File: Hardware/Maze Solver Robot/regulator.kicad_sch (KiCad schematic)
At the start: 0 parts

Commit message: Voltage Regulator
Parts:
- added C?: 220u, symbol Device:C_Polarized_Small_US
- added C?: 10u, symbol Device:C_Polarized_Small_US
- added R?: 240, symbol Device:R
- added R?: 390, symbol Device:R
- added U?: LM317L_SOT-89, Package_TO_SOT_SMD:SOT-89-3, symbol Regulator_Linear:LM317L_SOT-89
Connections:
- new net: R?.1, R?.2, U?.1 (ADJ)
- new net 3.3V: C?.1, R?.1, U?.2 (VO)
- new net GND: C?.2, C?.2, R?.2
- new net Input (Battery?): C?.1, U?.3 (VI)
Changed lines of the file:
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@@
 (kicad_sch (version 20211123) (generator eeschema)
   (paper "A4")
+  (junction (at 142.875 78.74) (diameter 0) (color 0 0 0 0)
+  )
+  (junction (at 170.815 64.77) (diameter 0) (color 0 0 0 0)
+  )
+  (junction (at 142.875 93.345) (diameter 0) (color 0 0 0 0)
+  )
+  (junction (at 159.385 64.77) (diameter 0) (color 0 0 0 0)
+  )
+  (junction (at 128.27 64.77) (diameter 0) (color 0 0 0 0)
+  )
+  (junction (at 128.27 93.345) (diameter 0) (color 0 0 0 0)
+  )
+  (wire (pts (xy 122.555 64.77) (xy 128.27 64.77))
+    (stroke (width 0) (type default) (color 0 0 0 0))
+  )
+  (wire (pts (xy 159.385 77.47) (xy 159.385 78.74))
+    (stroke (width 0) (type default) (color 0 0 0 0))
+  )
+  (wire (pts (xy 142.875 78.74) (xy 159.385 78.74))
+    (stroke (width 0) (type default) (color 0 0 0 0))
+  )
+  (wire (pts (xy 159.385 64.77) (xy 159.385 69.85))
+    (stroke (width 0) (type default) (color 0 0 0 0))
+  )
+  (wire (pts (xy 170.815 64.77) (xy 170.815 71.12))
+    (stroke (width 0) (type default) (color 0 0 0 0))
+  )
+  (wire (pts (xy 128.27 93.345) (xy 128.27 95.25))
+    (stroke (width 0) (type default) (color 0 0 0 0))
+  )
+  (wire (pts (xy 128.27 64.77) (xy 128.27 71.755))
+    (stroke (width 0) (type default) (color 0 0 0 0))
+  )
+  (wire (pts (xy 128.27 76.835) (xy 128.27 93.345))
+    (stroke (width 0) (type default) (color 0 0 0 0))
+  )
+  (wire (pts (xy 159.385 64.77) (xy 170.815 64.77))
+    (stroke (width 0) (type default) (color 0 0 0 0))
+  )
+  (wire (pts (xy 170.815 93.345) (xy 170.815 76.2))
+    (stroke (width 0) (type default) (color 0 0 0 0))
+  )
+  (wire (pts (xy 142.875 93.345) (xy 170.815 93.345))
+    (stroke (width 0) (type default) (color 0 0 0 0))
+  )
+  (wire (pts (xy 170.815 64.77) (xy 177.165 64.77))
+    (stroke (width 0) (type default) (color 0 0 0 0))
+  )
+  (wire (pts (xy 128.27 93.345) (xy 142.875 93.345))
+    (stroke (width 0) (type default) (color 0 0 0 0))
+  )
+  (wire (pts (xy 128.27 64.77) (xy 135.255 64.77))
+    (stroke (width 0) (type default) (color 0 0 0 0))
+  )
+  (wire (pts (xy 142.875 90.805) (xy 142.875 93.345))
+    (stroke (width 0) (type default) (color 0 0 0 0))
+  )
+  (wire (pts (xy 142.875 78.74) (xy 142.875 83.185))
+    (stroke (width 0) (type default) (color 0 0 0 0))
+  )
+  (wire (pts (xy 142.875 72.39) (xy 142.875 78.74))
+    (stroke (width 0) (type default) (color 0 0 0 0))
+  )
+  (wire (pts (xy 150.495 64.77) (xy 159.385 64.77))
+    (stroke (width 0) (type default) (color 0 0 0 0))
+  )
+  (global_label "3.3V" (shape output) (at 177.165 64.77 0) (fields_autoplaced)
+    (effects (font (size 1.27 1.27)) (justify left))
+    (property "Intersheet References" "${INTERSHEET_REFS}" (id 0) (at 183.6905 64.6906 0)
+      (effects (font (size 1.27 1.27)) (justify left) hide)
+    )
+  )
+  (global_label "Input (Battery?)" (shape input) (at 122.555 64.77 180) (fields_autoplaced)
+    (effects (font (size 1.27 1.27)) (justify right))
+    (property "Intersheet References" "${INTERSHEET_REFS}" (id 0) (at 104.9019 64.6906 0)
+      (effects (font (size 1.27 1.27)) (justify right) hide)
+    )
+  )
+  (symbol (lib_id "Device:C_Polarized_Small_US") (at 128.27 74.295 0) (unit 1)
+    (in_bom yes) (on_board yes)
+    (property "Reference" "C?" (id 0) (at 122.555 73.66 0)
+      (effects (font (size 1.27 1.27)) (justify left))
+    )
+    (property "Value" "220u" (id 1) (at 120.65 76.2 0)
+      (effects (font (size 1.27 1.27)) (justify left))
+    )
+    (property "Footprint" "" (id 2) (at 128.27 74.295 0)
+      (effects (font (size 1.27 1.27)) hide)
+    )
+    (property "Datasheet" "~" (id 3) (at 128.27 74.295 0)
+      (effects (font (size 1.27 1.27)) hide)
+    )
+    (pin "1")
+    (pin "2")
+  )
+  (symbol (lib_id "Regulator_Linear:LM317L_SOT-89") (at 142.875 64.77 0) (unit 1)
+    (in_bom yes) (on_board yes) (fields_autoplaced)
+    (property "Reference" "U?" (id 0) (at 142.875 57.15 0))
+    (property "Value" "LM317L_SOT-89" (id 1) (at 142.875 59.69 0))
+    (property "Footprint" "Package_TO_SOT_SMD:SOT-89-3" (id 2) (at 142.875 58.42 0)
+      (effects (font (size 1.27 1.27) italic) hide)
+    )
+    (property "Datasheet" "http://www.ti.com/lit/ds/symlink/lm317l.pdf" (id 3) (at 142.875 64.77 0)
+      (effects (font (size 1.27 1.27)) hide)
+    )
+    (pin "1")
+    (pin "2")
+    (pin "3")
+  )
+  (symbol (lib_id "Device:C_Polarized_Small_US") (at 170.815 73.66 0) (unit 1)
+    (in_bom yes) (on_board yes) (fields_autoplaced)
+    (property "Reference" "C?" (id 0) (at 173.99 71.9581 0)
+      (effects (font (size 1.27 1.27)) (justify left))
+    )
+    (property "Value" "10u" (id 1) (at 173.99 74.4981 0)
+      (effects (font (size 1.27 1.27)) (justify left))
+    )
+    (property "Footprint" "" (id 2) (at 170.815 73.66 0)
+      (effects (font (size 1.27 1.27)) hide)
+    )
+    (property "Datasheet" "~" (id 3) (at 170.815 73.66 0)
+      (effects (font (size 1.27 1.27)) hide)
+    )
+    (pin "1")
+    (pin "2")
+  )
+  (symbol (lib_id "Device:R") (at 159.385 73.66 0) (unit 1)
+    (in_bom yes) (on_board yes) (fields_autoplaced)
+    (property "Reference" "R?" (id 0) (at 161.29 72.3899 0)
+      (effects (font (size 1.27 1.27)) (justify left))
+    )
+    (property "Value" "240" (id 1) (at 161.29 74.9299 0)
+      (effects (font (size 1.27 1.27)) (justify left))
+    )
+    (property "Footprint" "" (id 2) (at 157.607 73.66 90)
+      (effects (font (size 1.27 1.27)) hide)
+    )
+    (property "Datasheet" "~" (id 3) (at 159.385 73.66 0)
+      (effects (font (size 1.27 1.27)) hide)
+    )
+    (pin "1")
+    (pin "2")
+  )
+  (symbol (lib_id "power:GND") (at 128.27 95.25 0) (unit 1)
+    (in_bom yes) (on_board yes) (fields_autoplaced)
+    (property "Reference" "#PWR?" (id 0) (at 128.27 101.6 0)
+      (effects (font (size 1.27 1.27)) hide)
+    )
+    (property "Value" "GND" (id 1) (at 128.27 99.695 0))
+    (property "Footprint" "" (id 2) (at 128.27 95.25 0)
+      (effects (font (size 1.27 1.27)) hide)
+    )
+    (property "Datasheet" "" (id 3) (at 128.27 95.25 0)
+      (effects (font (size 1.27 1.27)) hide)
+    )
+    (pin "1")
+  )
+  (symbol (lib_id "Device:R") (at 142.875 86.995 0) (unit 1)
+    (in_bom yes) (on_board yes) (fields_autoplaced)
+    (property "Reference" "R?" (id 0) (at 144.78 85.7249 0)
+      (effects (font (size 1.27 1.27)) (justify left))
+    )
+    (property "Value" "390" (id 1) (at 144.78 88.2649 0)
+      (effects (font (size 1.27 1.27)) (justify left))
+    )
+    (property "Footprint" "" (id 2) (at 141.097 86.995 90)
+      (effects (font (size 1.27 1.27)) hide)
+    )
+    (property "Datasheet" "~" (id 3) (at 142.875 86.995 0)
+      (effects (font (size 1.27 1.27)) hide)
+    )
+    (pin "1")
+    (pin "2")
+  )
 )

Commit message: Add final changes
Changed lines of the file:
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@@
     (stroke (width 0) (type default) (color 0 0 0 0))
   )
-  (global_label "3.3V" (shape output) (at 177.165 64.77 0) (fields_autoplaced)
+  (hierarchical_label "Input (Battery?)" (shape input) (at 122.555 64.77 180)
+    (effects (font (size 1.27 1.27)) (justify right))
+  )
+  (hierarchical_label "3.3V" (shape output) (at 177.165 64.77 0)
     (effects (font (size 1.27 1.27)) (justify left))
-    (property "Intersheet References" "${INTERSHEET_REFS}" (id 0) (at 183.6905 64.6906 0)
-      (effects (font (size 1.27 1.27)) (justify left) hide)
-    )
-  )
-  (global_label "Input (Battery?)" (shape input) (at 122.555 64.77 180) (fields_autoplaced)
-    (effects (font (size 1.27 1.27)) (justify right))
-    (property "Intersheet References" "${INTERSHEET_REFS}" (id 0) (at 104.9019 64.6906 0)
-      (effects (font (size 1.27 1.27)) (justify right) hide)
-    )
   )
   (symbol (lib_id "Device:C_Polarized_Small_US") (at 128.27 74.295 0) (unit 1)

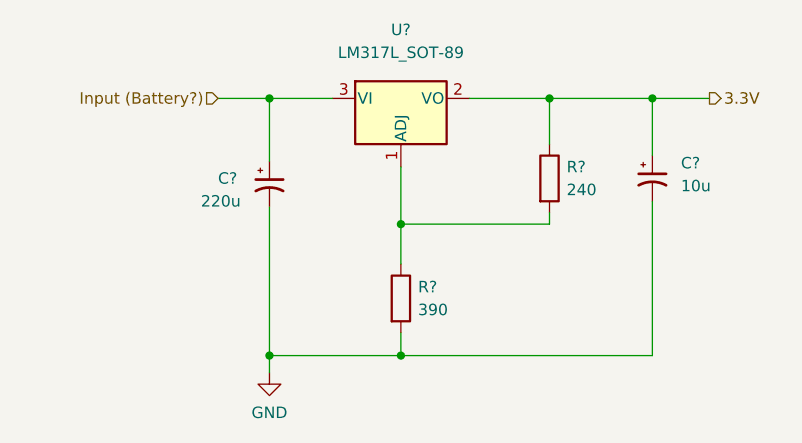
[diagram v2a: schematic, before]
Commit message: Add comments to schematics
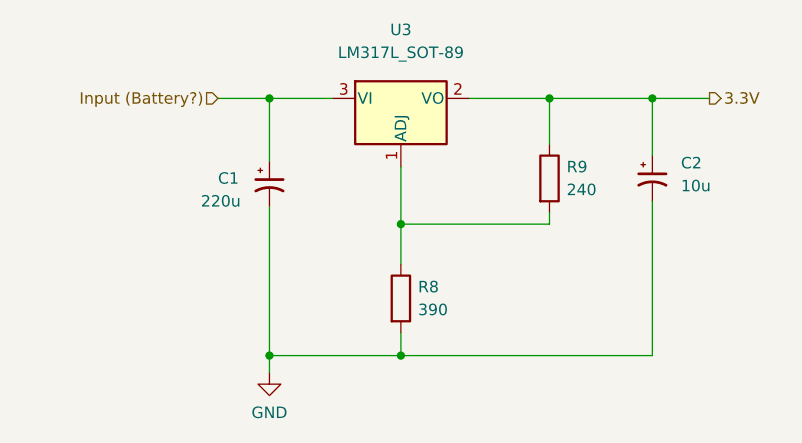
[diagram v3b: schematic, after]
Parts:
- gave numbers to parts that had none: 5
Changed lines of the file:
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@@
   (symbol (lib_id "Device:C_Polarized_Small_US") (at 128.27 74.295 0) (unit 1)
     (in_bom yes) (on_board yes)
-    (property "Reference" "C?" (id 0) (at 122.555 73.66 0)
+    (property "Reference" "C1" (id 0) (at 122.555 73.66 0)
       (effects (font (size 1.27 1.27)) (justify left))
     )
@@
   (symbol (lib_id "Regulator_Linear:LM317L_SOT-89") (at 142.875 64.77 0) (unit 1)
     (in_bom yes) (on_board yes) (fields_autoplaced)
-    (property "Reference" "U?" (id 0) (at 142.875 57.15 0))
+    (property "Reference" "U3" (id 0) (at 142.875 57.15 0))
     (property "Value" "LM317L_SOT-89" (id 1) (at 142.875 59.69 0))
     (property "Footprint" "Package_TO_SOT_SMD:SOT-89-3" (id 2) (at 142.875 58.42 0)
@@
   (symbol (lib_id "Device:C_Polarized_Small_US") (at 170.815 73.66 0) (unit 1)
     (in_bom yes) (on_board yes) (fields_autoplaced)
-    (property "Reference" "C?" (id 0) (at 173.99 71.9581 0)
+    (property "Reference" "C2" (id 0) (at 173.99 71.9581 0)
       (effects (font (size 1.27 1.27)) (justify left))
     )
@@
   (symbol (lib_id "Device:R") (at 159.385 73.66 0) (unit 1)
     (in_bom yes) (on_board yes) (fields_autoplaced)
-    (property "Reference" "R?" (id 0) (at 161.29 72.3899 0)
+    (property "Reference" "R9" (id 0) (at 161.29 72.3899 0)
       (effects (font (size 1.27 1.27)) (justify left))
     )
@@
   (symbol (lib_id "power:GND") (at 128.27 95.25 0) (unit 1)
     (in_bom yes) (on_board yes) (fields_autoplaced)
-    (property "Reference" "#PWR?" (id 0) (at 128.27 101.6 0)
+    (property "Reference" "#PWR09" (id 0) (at 128.27 101.6 0)
       (effects (font (size 1.27 1.27)) hide)
     )
@@
   (symbol (lib_id "Device:R") (at 142.875 86.995 0) (unit 1)
     (in_bom yes) (on_board yes) (fields_autoplaced)
-    (property "Reference" "R?" (id 0) (at 144.78 85.7249 0)
+    (property "Reference" "R8" (id 0) (at 144.78 85.7249 0)
       (effects (font (size 1.27 1.27)) (justify left))
     )
